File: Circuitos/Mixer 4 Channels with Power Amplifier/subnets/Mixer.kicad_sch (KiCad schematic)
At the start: 14 parts, among them J1 XLR3, J2 AudioJack 3.5mm, J3 AudioJack 6.35mm, SW2 SW_Nidec_CAS-120A1, SW3 SW_Push, U8 ${SIM.PARAMS}

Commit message: Correcciones en etapas y respaldo fotos simulación
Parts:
- Rf: value 820 -> 1k
- Ri1, Ri2, Ri3, Ri4: value 2.2k -> 2.7k
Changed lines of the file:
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@@
 			)
 		)
-		(property "Value" "2.2k"
+		(property "Value" "2.7k"
 			(at 205.74 124.46 90)
 			(effects
@@
 			)
 		)
-		(property "Value" "2.2k"
+		(property "Value" "2.7k"
 			(at 204.4699 134.62 0)
 			(effects
@@
 			)
 		)
-		(property "Value" "2.2k"
+		(property "Value" "2.7k"
 			(at 204.4699 139.7 0)
 			(effects
@@
 			)
 		)
-		(property "Value" "820"
+		(property "Value" "1k"
 			(at 219.7099 119.38 90)
 			(effects
@@
 			)
 		)
-		(property "Value" "2.2k"
+		(property "Value" "2.7k"
 			(at 204.4699 129.54 0)
 			(effects

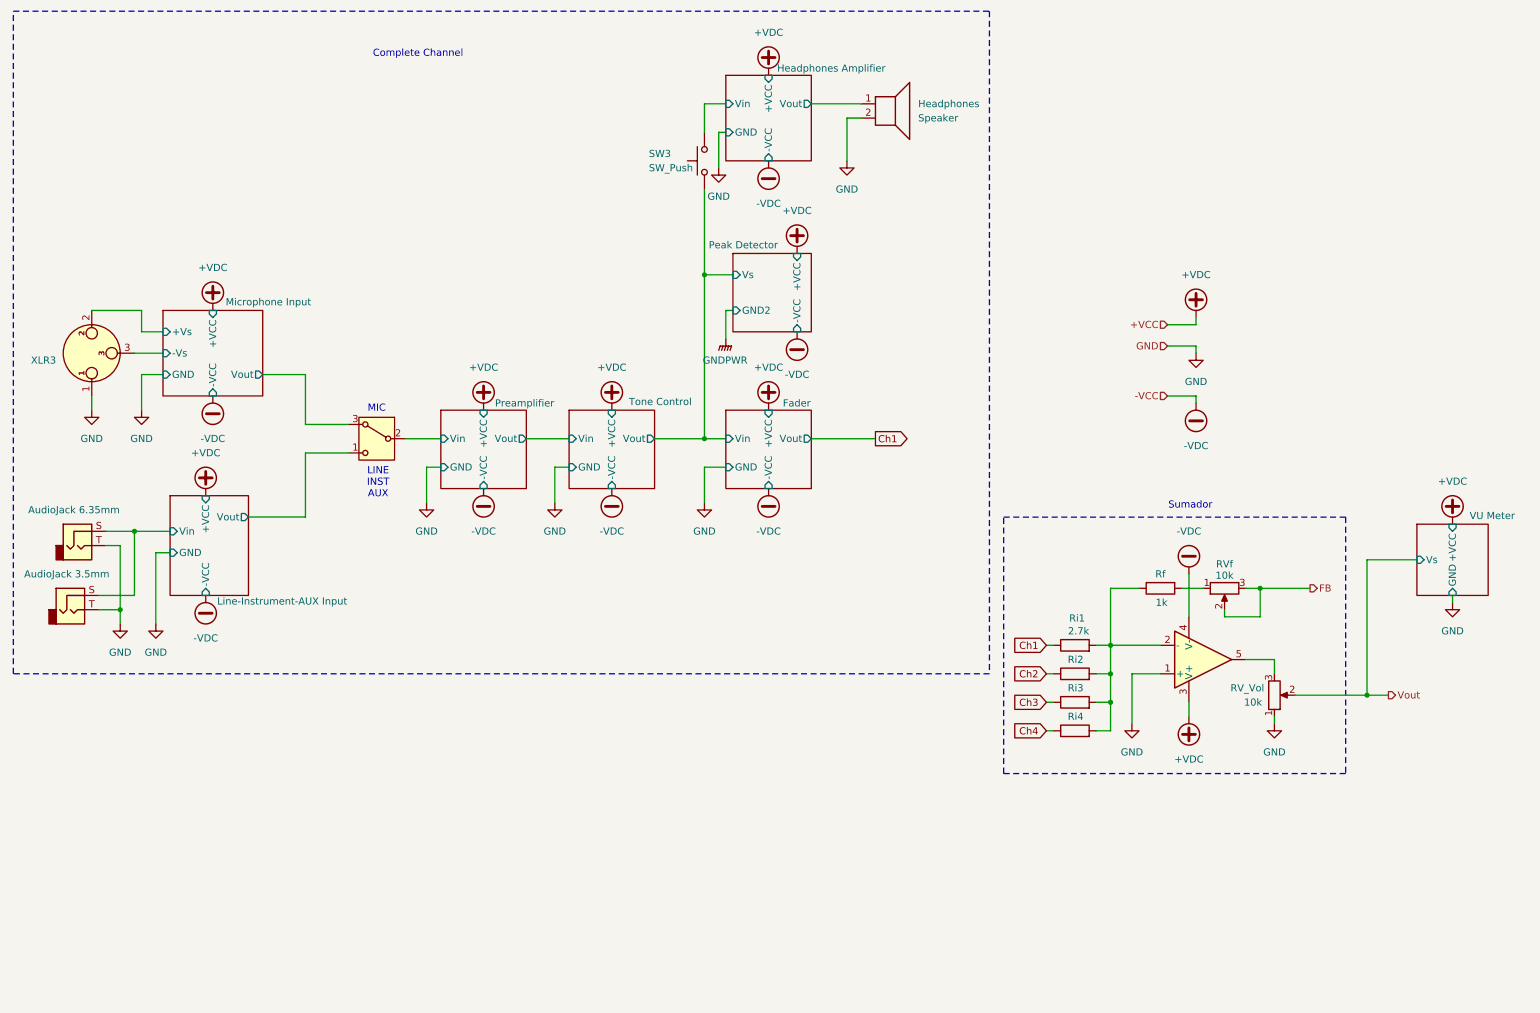
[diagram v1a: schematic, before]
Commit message: Correcciones y modificaciones en fuente, amp auriculares y simul completa
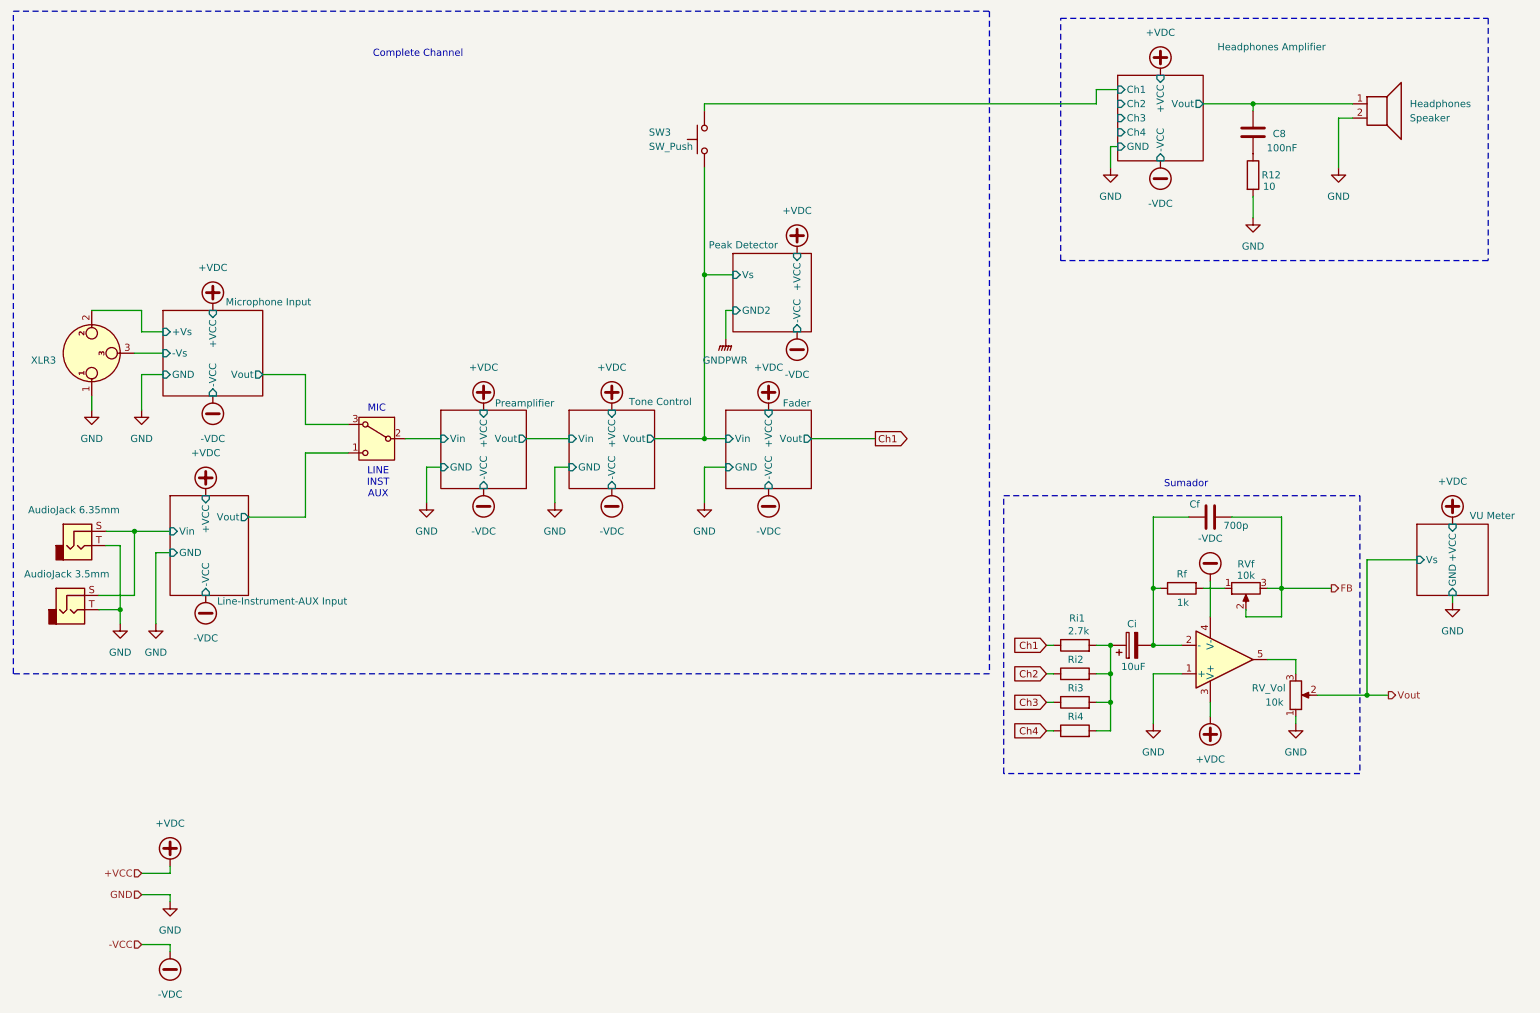
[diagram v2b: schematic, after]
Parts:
- added C8: 100nF, symbol Device:C
- added Cf: 700p, symbol Device:C
- added Ci: 10uF, symbol Device:C_Polarized
- added R12: 10, symbol Device:R
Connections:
- net FB: now also Cf.2
- net GND: now also R12.2
- net Headphones Amplifier/Vout: now also C8.2
- net at Ri1.2, Ri2.2, Ri3.2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: now also Ci.1; no longer Rf.1, U8.2 (-)
- net Headphones Amplifier/Vin renamed Headphones Amplifier/Ch1
- new net: C8.1, R12.1
- new net: Cf.1, Ci.2, Rf.1, U8.2 (-)
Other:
- sheet Headphones Amplifier ports: added Ch1, Ch2, Ch3, Ch4; removed Vin
- moved on the sheet: Headphones, RV_Vol, RVf, Rf, SW3
